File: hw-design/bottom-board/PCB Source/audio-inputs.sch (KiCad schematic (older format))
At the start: 83 parts, among them J7 NYS215, J8 NYS215, Q10 J110, Q11 J110, Q12 2N7002, Q13 2N7002, Q14 J110, Q15 J110, Q16 2N7002, Q9 2N7002, U8 LM4562

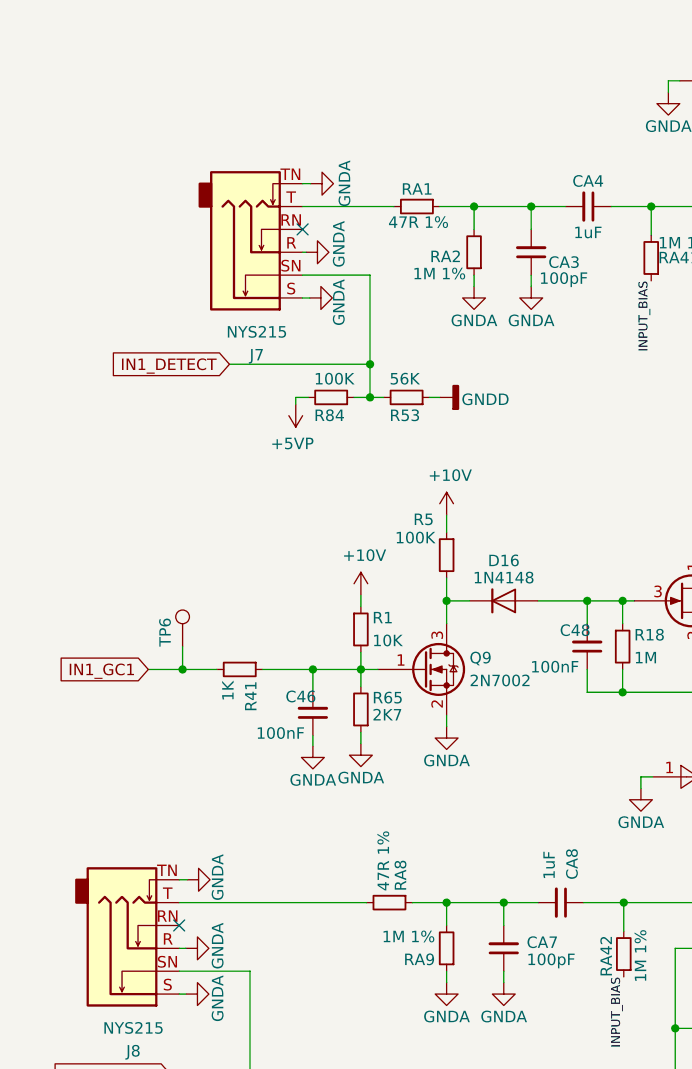
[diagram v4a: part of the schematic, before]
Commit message: fix DAC symbol + GND
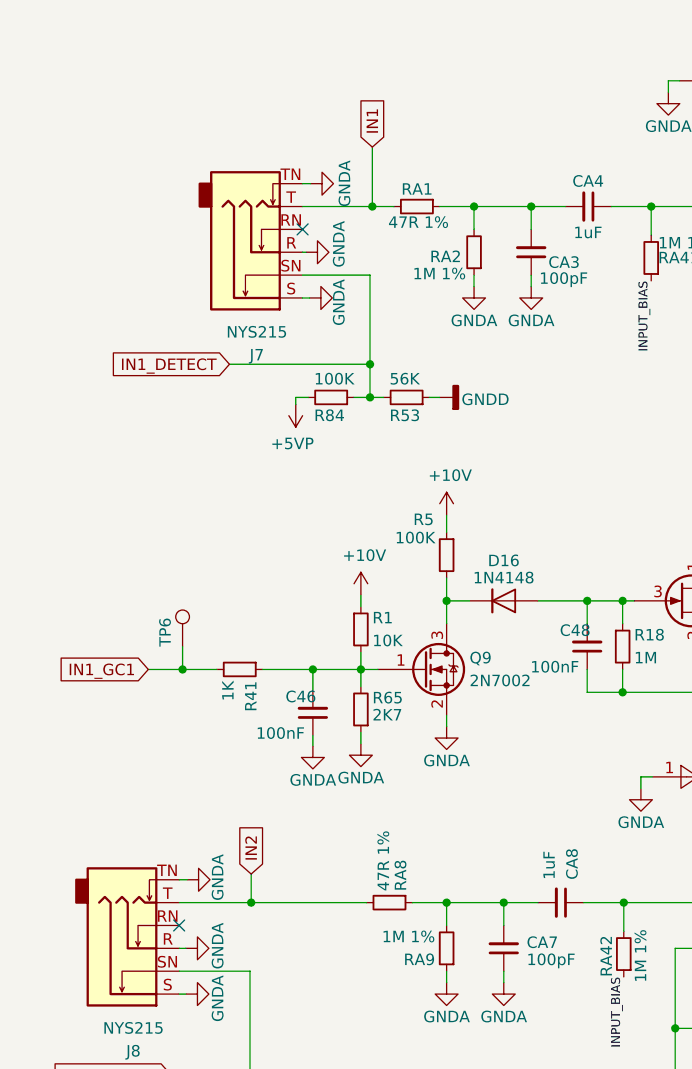
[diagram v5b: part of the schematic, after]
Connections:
- net IN1: now reaches J7.T, RA1.2
- net IN2: now reaches J8.T, RA8.2
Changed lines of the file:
@@
 IN1_DETECT
 Wire Wire Line
-	2495 1365 2095 1365
+	2495 1365 2400 1365
 Wire Wire Line
 	2320 2200 2390 2200
@@
 	1865 5360 1925 5360
 Wire Wire Line
-	1555 4410 2375 4410
+	1555 4410 1870 4410
 Wire Wire Line
 	1555 4710 1865 4710
@@
 Wire Wire Line
 	8660 4590 8660 4710
+Text GLabel 2400 1105 1    50   Input ~ 0
+IN1
+Wire Wire Line
+	2400 1105 2400 1365
+Connection ~ 2400 1365
+Wire Wire Line
+	2400 1365 2095 1365
+Text GLabel 1870 4285 1    50   Input ~ 0
+IN2
+Wire Wire Line
+	1870 4285 1870 4410
+Connection ~ 1870 4410
+Wire Wire Line
+	1870 4410 2375 4410
 $EndSCHEMATC

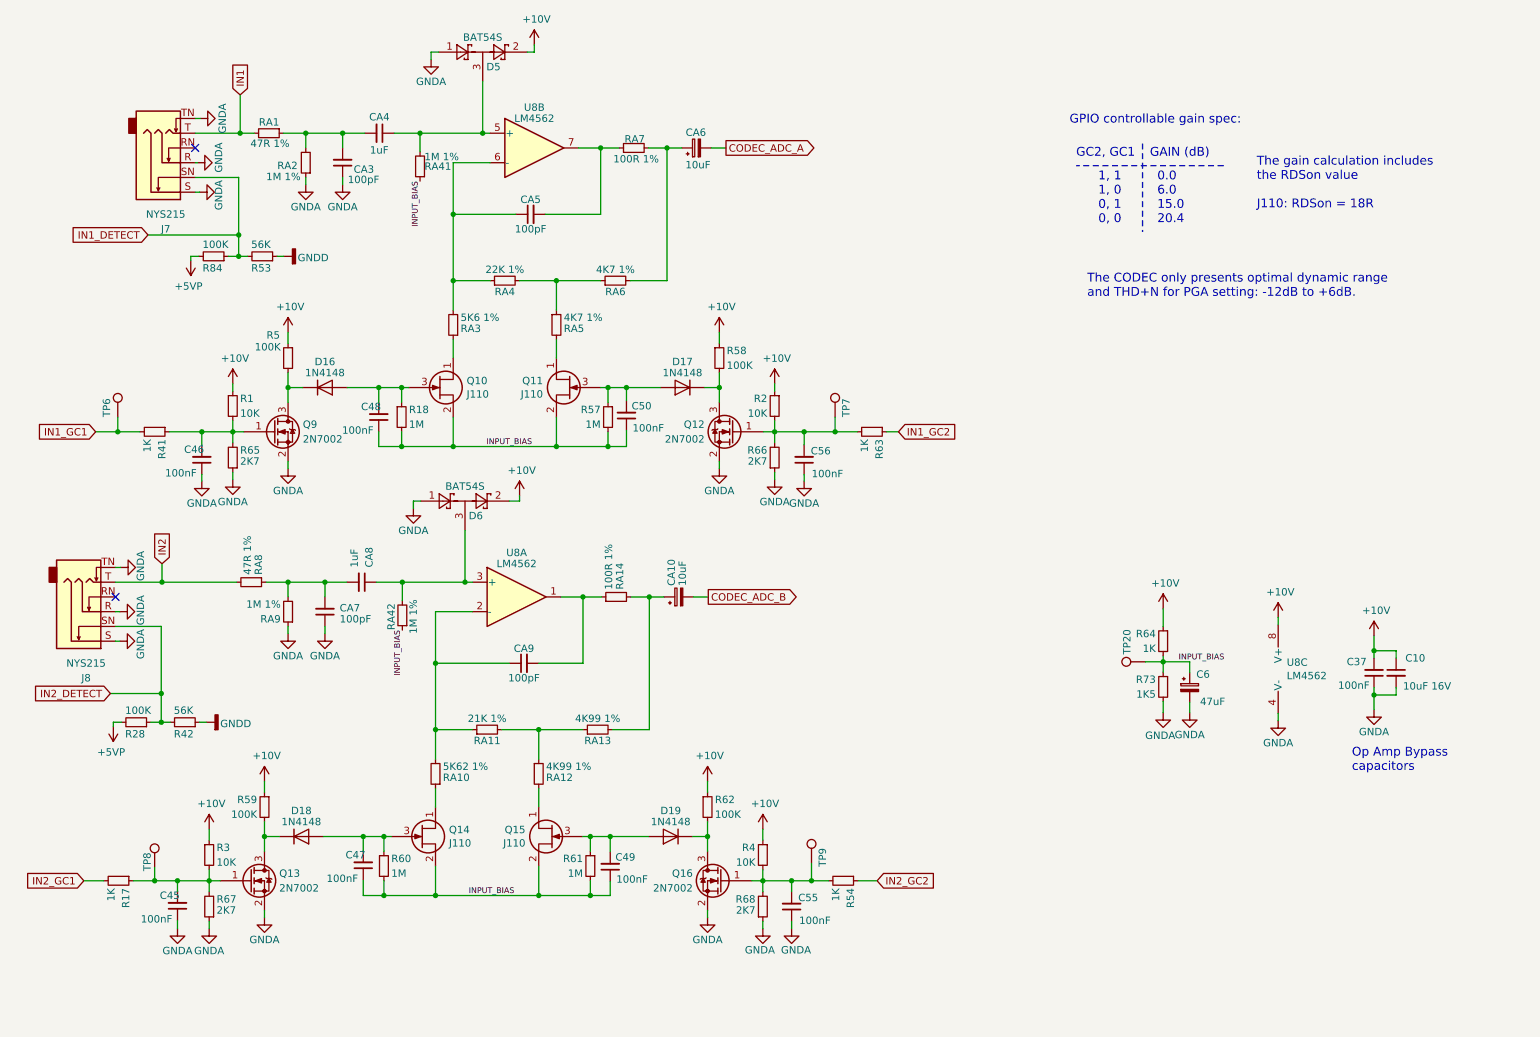
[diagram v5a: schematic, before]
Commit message: update all MPN's to match the Dwarf
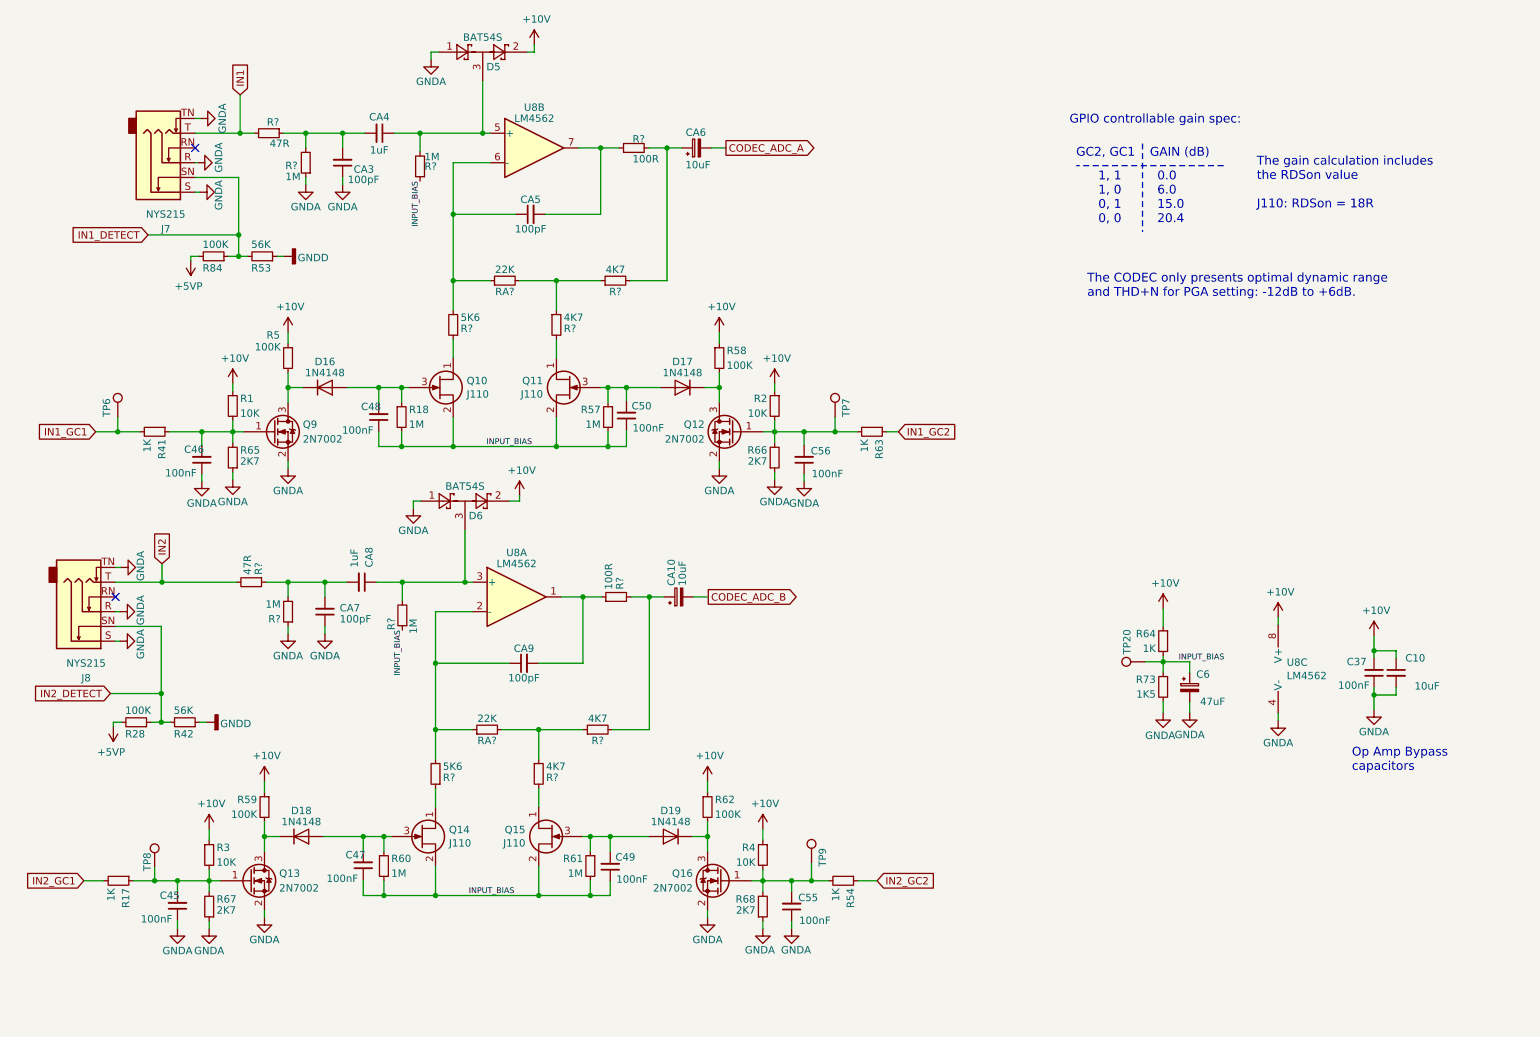
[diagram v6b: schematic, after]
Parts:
- C10: value 10uF 16V -> 10uF; MPN CL21A106KOFNNNE -> GRM219R61E106KA12D
- R17, R41, R54, R63, R64: MPN (none) -> ERJ-PB3D1001V
- R18: MPN (none) -> RT0603BRD071ML
- R28, R84: MPN (none) -> RMCF0603JT100K
- R42, R53: MPN (none) -> RT0603DRD0756KL
- R65, R66, R67, R68: MPN RMCF0603JT2K70 -> CRGCQ0603F2K7
- R73: MPN (none) -> CRGCQ0603F1K5
- R?: renamed from RA1; value 47R 1% -> 47R
- R?: renamed from RA2; value 1M 1% -> 1M
- R?: renamed from RA3; value 5K6 1% -> 5K6; MPN (none) -> ERA-3AED562V
- R?: renamed from RA6; value 4K7 1% -> 4K7; MPN (none) -> RT0603DRE074K7L
- R?: renamed from RA7; value 100R 1% -> 100R; MPN RR0816P-101-D -> RT0603DRD07100RL
- R?: renamed from RA4; value 22K 1% -> 22K; MPN (none) -> RT0603DRD0722KL
- R?: renamed from RA5; value 4K7 1% -> 4K7; MPN (none) -> RT0603DRE074K7L
- R?: renamed from RA8; value 47R 1% -> 47R
- R?: renamed from RA9; value 1M 1% -> 1M
- R?: renamed from RA14; value 100R 1% -> 100R; MPN RR0816P-101-D -> RT0603DRD07100RL
- R?: renamed from RA41; value 1M 1% -> 1M
- R?: renamed from RA42; value 1M 1% -> 1M
- R?: renamed from RA11; value 21K 1% -> 22K; MPN RR0816P-2102-D-32C -> RT0603DRD0722KL
- R?: renamed from RA13; value 4K99 1% -> 4K7; MPN ERA-3AEB4991V -> RT0603DRE074K7L
- R?: renamed from RA10; value 5K62 1% -> 5K6; MPN ERA-3AEB5621V -> ERA-3AED562V
- R?: renamed from RA12; value 4K99 1% -> 4K7; MPN ERA-3AEB4991V -> RT0603DRE074K7L

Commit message: update fabrication files
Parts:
- gave numbers to parts that had none: 16
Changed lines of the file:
@@
 $EndDescr
 $Comp
-L bottom-board-rescue:R_Small-Device R?
+L bottom-board-rescue:R_Small-Device R92
 U 1 1 5B52CAFF
 P 2595 1365
-F 0 "R?" V 2520 1435 50  0000 R CNN
+F 0 "R92" V 2520 1435 50  0000 R CNN
 F 1 "47R" V 2665 1505 50  0000 R CNN
 F 2 "Resistor_SMD:R_0603_1608Metric" H 2595 1365 60  0001 C CNN
@@
 $EndComp
 $Comp
-L bottom-board-rescue:R_Small-Device R?
+L bottom-board-rescue:R_Small-Device R94
 U 1 1 5B52CB07
 P 2845 1565
-F 0 "R?" H 2900 1585 50  0000 L CNN
+F 0 "R94" H 2900 1585 50  0000 L CNN
 F 1 "1M" H 2880 1660 50  0000 L CNN
 F 2 "Resistor_SMD:R_0603_1608Metric" H 2845 1565 60  0001 C CNN
@@
 $EndComp
 $Comp
-L bottom-board-rescue:R_Small-Device R?
+L bottom-board-rescue:R_Small-Device R98
 U 1 1 5B52CB0F
 P 3845 2665
-F 0 "R?" H 3795 2690 50  0000 R CNN
+F 0 "R98" H 3795 2690 50  0000 R CNN
 F 1 "5K6" H 3795 2615 50  0000 R CNN
 F 2 "Resistor_SMD:R_0603_1608Metric" H 3845 2665 60  0001 C CNN
@@
 $EndComp
 $Comp
-L bottom-board-rescue:R_Small-Device R?
+L bottom-board-rescue:R_Small-Device R104
 U 1 1 5B52CB1F
 P 4945 2365
-F 0 "R?" V 4870 2365 50  0000 C CNN
+F 0 "R104" V 4870 2365 50  0000 C CNN
 F 1 "4K7" V 5020 2365 50  0000 C CNN
 F 2 "Resistor_SMD:R_0603_1608Metric" H 4945 2365 60  0001 C CNN
@@
 $EndComp
 $Comp
-L bottom-board-rescue:R_Small-Device R?
+L bottom-board-rescue:R_Small-Device R106
 U 1 1 5B52CB2F
 P 5070 1465
-F 0 "R?" V 5130 1390 50  0000 L CNN
+F 0 "R106" V 5130 1390 50  0000 L CNN
 F 1 "100R" V 4995 1295 50  0000 L CNN
 F 2 "Resistor_SMD:R_0603_1608Metric" H 5070 1465 60  0001 C CNN
@@
 P 4195 2365
 AR Path="/54F7244B/5B6A7A98" Ref="RA?"  Part="1"
-AR Path="/54F72C8D/5B6A7A98" Ref="R?"  Part="1"
-F 0 "R?" V 4120 2365 50  0000 C CNN
+AR Path="/54F72C8D/5B6A7A98" Ref="R100"  Part="1"
+F 0 "R100" V 4120 2365 50  0000 C CNN
 F 1 "22K" V 4270 2365 50  0000 C CNN
 F 2 "Resistor_SMD:R_0603_1608Metric" H 4195 2365 50  0001 C CNN
@@
 Connection ~ 3925 4410
 $Comp
-L bottom-board-rescue:R_Small-Device R?
+L bottom-board-rescue:R_Small-Device R102
 U 1 1 5B6B74CD
 P 4545 2665
-F 0 "R?" H 4595 2640 50  0000 L CNN
+F 0 "R102" H 4595 2640 50  0000 L CNN
 F 1 "4K7" H 4595 2715 50  0000 L CNN
 F 2 "Resistor_SMD:R_0603_1608Metric" H 4545 2665 60  0001 C CNN
@@
 $EndComp
 $Comp
-L bottom-board-rescue:R_Small-Device R?
+L bottom-board-rescue:R_Small-Device R91
 U 1 1 5B6C0073
 P 2475 4410
-F 0 "R?" H 2425 4460 50  0000 R CNN
+F 0 "R91" H 2425 4460 50  0000 R CNN
 F 1 "47R" H 2425 4385 50  0000 R CNN
 F 2 "Resistor_SMD:R_0603_1608Metric" H 2475 4410 60  0001 C CNN
@@
 $EndComp
 $Comp
-L bottom-board-rescue:R_Small-Device R?
+L bottom-board-rescue:R_Small-Device R93
 U 1 1 5B6C2019
 P 2725 4610
-F 0 "R?" H 2775 4660 50  0000 L CNN
+F 0 "R93" H 2775 4660 50  0000 L CNN
 F 1 "1M" H 2775 4560 50  0000 L CNN
 F 2 "Resistor_SMD:R_0603_1608Metric" H 2725 4610 60  0001 C CNN
@@
 $EndComp
 $Comp
-L bottom-board-rescue:R_Small-Device R?
+L bottom-board-rescue:R_Small-Device R105
 U 1 1 5B6C8FDD
 P 4950 4510
-F 0 "R?" H 5000 4485 50  0000 L CNN
+F 0 "R105" H 5000 4485 50  0000 L CNN
 F 1 "100R" H 5000 4560 50  0000 L CNN
 F 2 "Resistor_SMD:R_0603_1608Metric" H 4950 4510 60  0001 C CNN
@@
 	4545 2890 4545 2765
 $Comp
-L bottom-board-rescue:R_Small-Device R?
+L bottom-board-rescue:R_Small-Device R96
 U 1 1 5BCC6E02
 P 3620 1590
-F 0 "R?" H 3590 1590 50  0000 R CNN
+F 0 "R96" H 3590 1590 50  0000 R CNN
 F 1 "1M" H 3590 1525 50  0000 R CNN
 F 2 "Resistor_SMD:R_0603_1608Metric" H 3620 1590 60  0001 C CNN
@@
 INPUT_BIAS
 $Comp
-L bottom-board-rescue:R_Small-Device R?
+L bottom-board-rescue:R_Small-Device R95
 U 1 1 5BCE4FCB
 P 3500 4635
-F 0 "R?" V 3575 4735 50  0000 R CNN
+F 0 "R95" V 3575 4735 50  0000 R CNN
 F 1 "1M" V 3425 4760 50  0000 R CNN
 F 2 "Resistor_SMD:R_0603_1608Metric" H 3500 4635 60  0001 C CNN
@@
 P 4075 5410
 AR Path="/54F7244B/5C3BF4A5" Ref="RA?"  Part="1"
-AR Path="/54F72C8D/5C3BF4A5" Ref="R?"  Part="1"
-F 0 "R?" V 4000 5410 50  0000 C CNN
+AR Path="/54F72C8D/5C3BF4A5" Ref="R99"  Part="1"
+F 0 "R99" V 4000 5410 50  0000 C CNN
 F 1 "22K" V 4150 5410 50  0000 C CNN
 F 2 "Resistor_SMD:R_0603_1608Metric" H 4075 5410 50  0001 C CNN
@@
 $EndComp
 $Comp
-L bottom-board-rescue:R_Small-Device R?
+L bottom-board-rescue:R_Small-Device R103
 U 1 1 5C3BF57D
 P 4825 5410
-F 0 "R?" V 4750 5410 50  0000 C CNN
+F 0 "R103" V 4750 5410 50  0000 C CNN
 F 1 "4K7" V 4900 5410 50  0000 C CNN
 F 2 "Resistor_SMD:R_0603_1608Metric" H 4825 5410 60  0001 C CNN
@@
 $EndComp
 $Comp
-L bottom-board-rescue:R_Small-Device R?
+L bottom-board-rescue:R_Small-Device R97
 U 1 1 5C3C120E
 P 3725 5710
-F 0 "R?" H 3675 5735 50  0000 R CNN
+F 0 "R97" H 3675 5735 50  0000 R CNN
 F 1 "5K6" H 3675 5660 50  0000 R CNN
 F 2 "Resistor_SMD:R_0603_1608Metric" H 3725 5710 60  0001 C CNN
@@
 $EndComp
 $Comp
-L bottom-board-rescue:R_Small-Device R?
+L bottom-board-rescue:R_Small-Device R101
 U 1 1 5C3C12F4
 P 4425 5710
-F 0 "R?" H 4475 5685 50  0000 L CNN
+F 0 "R101" H 4475 5685 50  0000 L CNN
 F 1 "4K7" H 4475 5760 50  0000 L CNN
 F 2 "Resistor_SMD:R_0603_1608Metric" H 4425 5710 60  0001 C CNN
